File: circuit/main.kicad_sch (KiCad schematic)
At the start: 15 parts, among them IC1 PIC16F1778-I_SP, J1 Conn_01x06_Pin, M1 Motor_DC, M2 Motor_DC, Q1 MP4212_Q_, Q2 MP4212_Q_, SW1 SW_SPDT

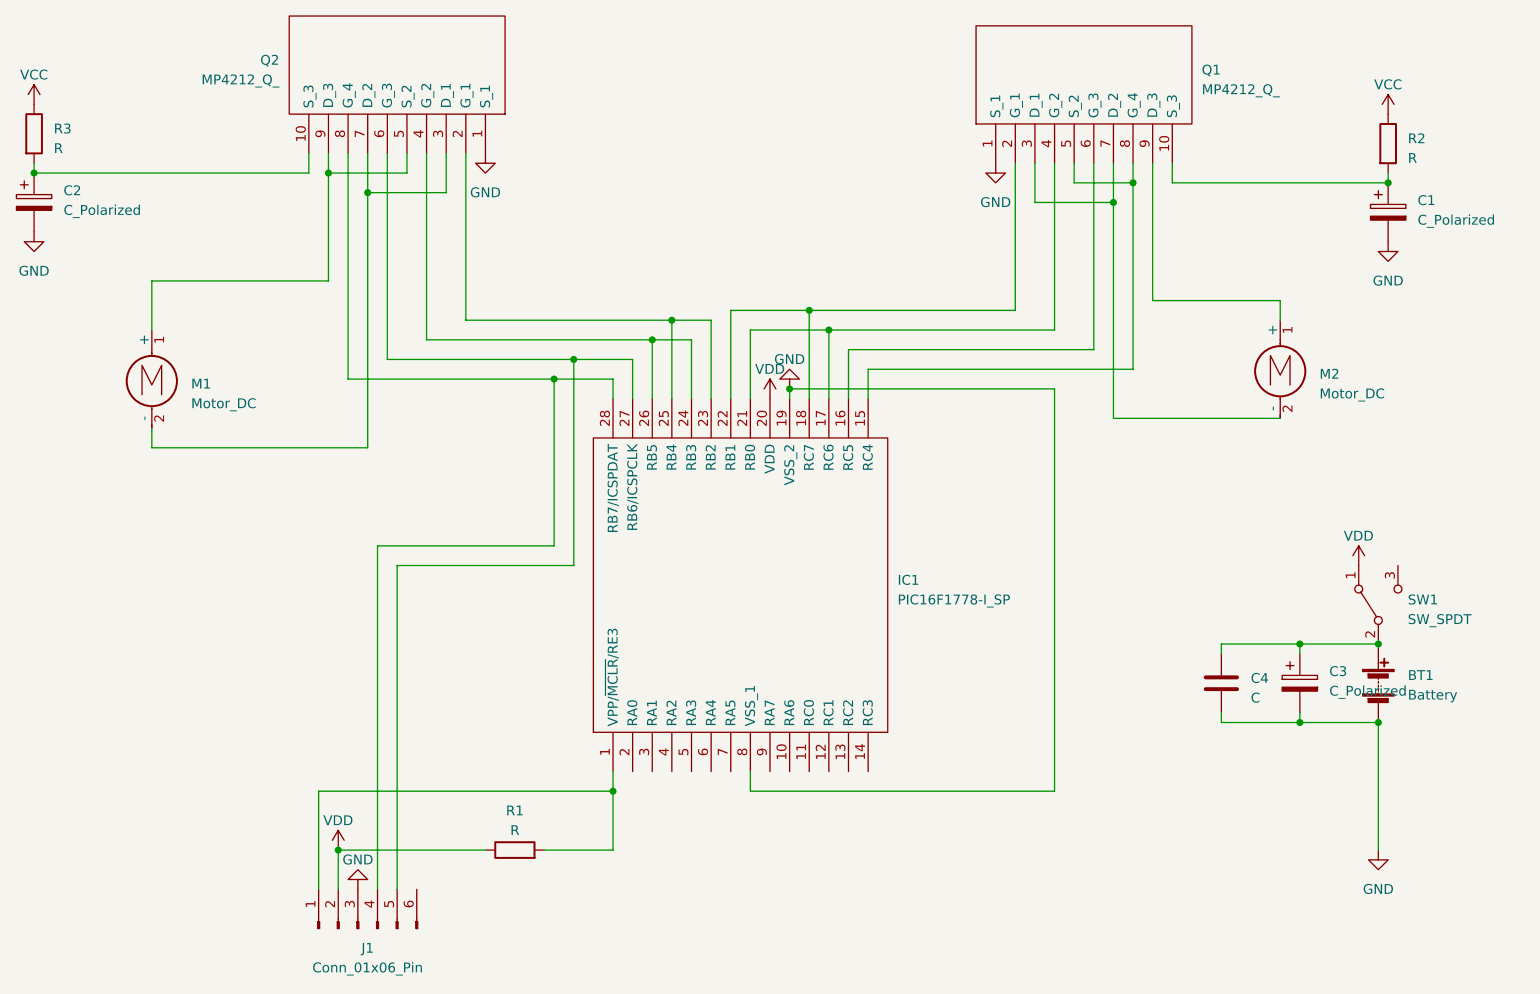
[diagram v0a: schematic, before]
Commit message: fix motors
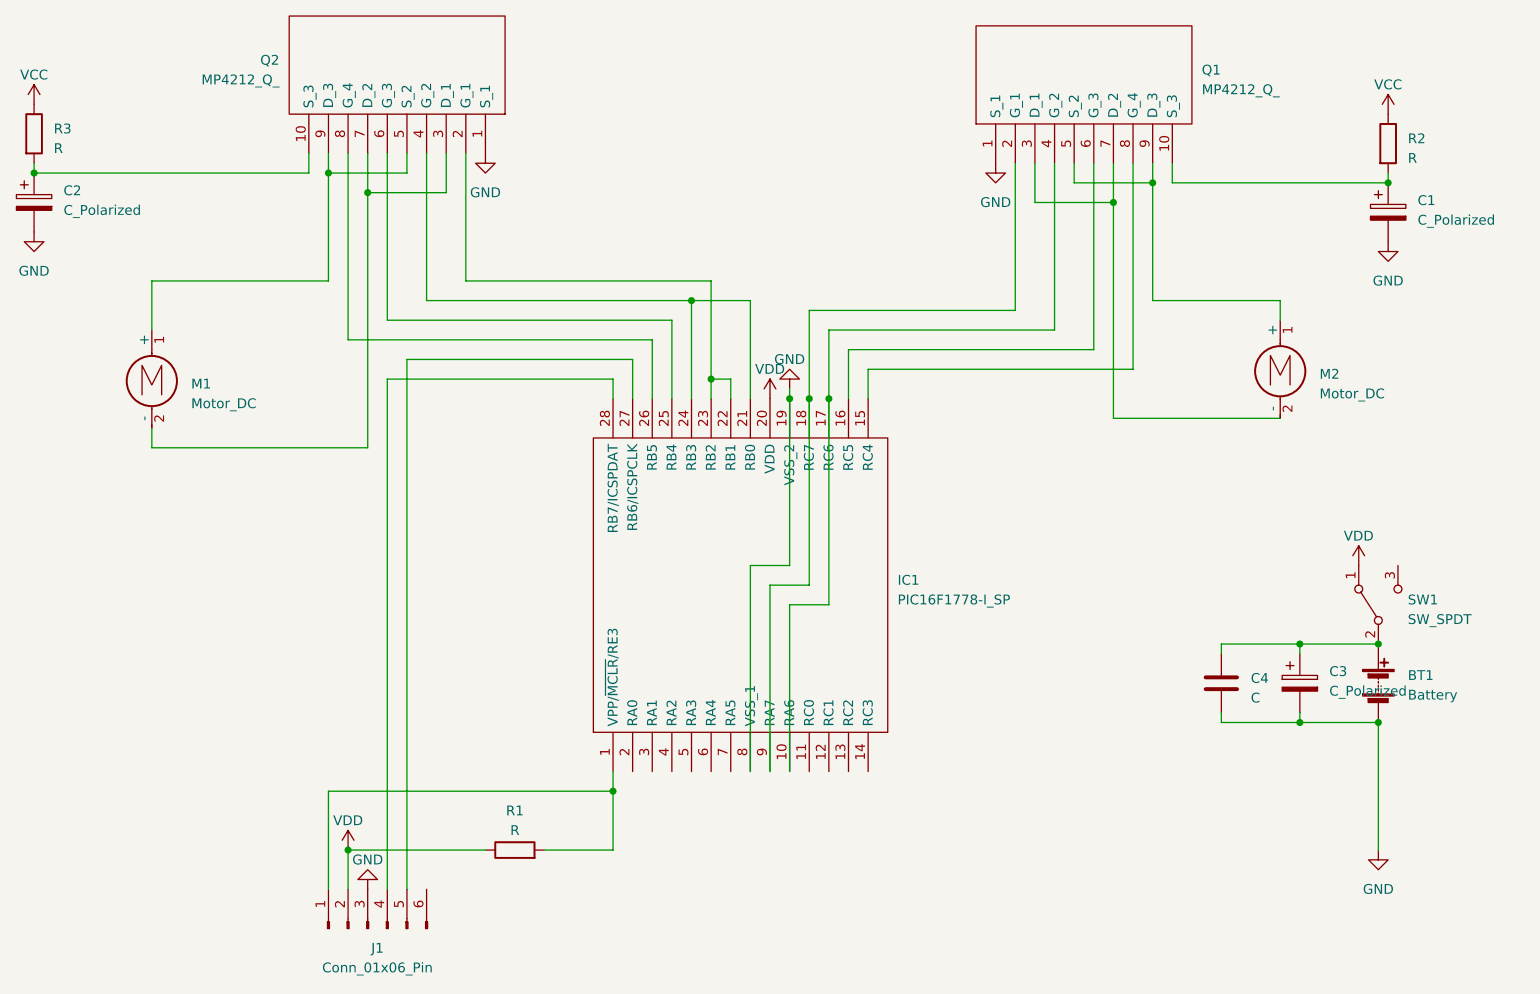
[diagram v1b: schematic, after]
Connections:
- net at IC1.18 (RC7), Q1.2 (G_1): now also IC1.9 (RA7); no longer IC1.22 (RB1)
- net at IC1.17 (RC6), Q1.4 (G_2): now also IC1.10 (RA6); no longer IC1.21 (RB0)
- net at IC1.15 (RC4), Q1.8 (G_4): no longer Q1.5 (S_2)
- net at M2.1 (+), Q1.9 (D_3): now also Q1.5 (S_2)
- net at IC1.23 (RB2), Q2.2 (G_1): now also IC1.22 (RB1); no longer IC1.25 (RB4)
- net at IC1.24 (RB3), Q2.4 (G_2): now also IC1.21 (RB0); no longer IC1.26 (RB5)
- net at IC1.27 (RB6/ICSPCLK), J1.5 (Pin_5): no longer Q2.6 (G_3)
- net at IC1.28 (RB7/ICSPDAT), J1.4 (Pin_4): no longer Q2.8 (G_4)
- new net: IC1.25 (RB4), Q2.6 (G_3)
- new net: IC1.26 (RB5), Q2.8 (G_4)
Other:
- moved on the sheet: J1

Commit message: circuit rc1
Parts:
- added D1, D2, D3, D4: LED, LED_THT:LED_D3.0mm, symbol Device:LED
- added J2: Conn_01x06_Pin, Connector_PinHeader_2.54mm:PinHeader_1x06_P2.54mm_Vertical, symbol Connector:Conn_01x06_Pin
- added R4, R5, R6, R7: R, Resistor_THT:R_Axial_DIN0207_L6.3mm_D2.5mm_P7.62mm_Horizontal, symbol Device:R
- BT1, M1, M2: footprint (none) -> Connector_PinHeader_2.54mm:PinHeader_1x02_P2.54mm_Horizontal
- C1, C2, C3: footprint (none) -> Capacitor_THT:CP_Radial_D5.0mm_P2.00mm
- C4: footprint (none) -> Capacitor_THT:C_Disc_D5.0mm_W2.5mm_P5.00mm
- IC1: footprint Samacsys:DIP794W56P254L3486H508Q28N -> Package_DIP:DIP-28_W7.62mm_LongPads
- J1: footprint (none) -> Connector_PinHeader_2.54mm:PinHeader_1x06_P2.54mm_Vertical
- R1: footprint (none) -> Resistor_THT:R_Axial_DIN0207_L6.3mm_D2.5mm_P7.62mm_Horizontal
- R2, R3: footprint (none) -> Resistor_THT:R_Axial_DIN0309_L9.0mm_D3.2mm_P12.70mm_Horizontal
- SW1: footprint (none) -> seik:ToggleSW_3pin
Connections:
- net VDD is gone; now on net VCC: IC1.20 (VDD), J1.2 (Pin_2), R1.1, SW1.1 (A)
- net GND: now also J2.1 (Pin_1), R4.2, R5.2, R6.2, R7.2
- net at IC1.11 (RC0): now also D1.2 (A)
- net at IC1.12 (RC1): now also D2.2 (A)
- net at IC1.13 (RC2): now also D3.2 (A)
- net at IC1.14 (RC3): now also D4.2 (A)
- net at IC1.3 (RA1): now also J2.6 (Pin_6)
- net at IC1.4 (RA2): now also J2.5 (Pin_5)
- net at IC1.5 (RA3): now also J2.4 (Pin_4)
- net at IC1.6 (RA4): now also J2.3 (Pin_3)
- net at IC1.7 (RA5): now also J2.2 (Pin_2)
- new net: D4.1 (K), R7.1
- new net: D2.1 (K), R5.1
- new net: D3.1 (K), R6.1
- new net: D1.1 (K), R4.1
- no-connect marks 0 -> 2
